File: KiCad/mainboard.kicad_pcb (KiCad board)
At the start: 2 copper layers, 139.7 x 83.8 mm, 60 parts, among them J1 Arduino_Nano_Header, P1 CONN_02X13, P2 CONN_02X13, P3 USB_B, P4 CONN_01X04, P5 CONN_01X02, P6 CONN_01X02, P7 CONN_01X02, U1 74LS165, U2 74LS165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

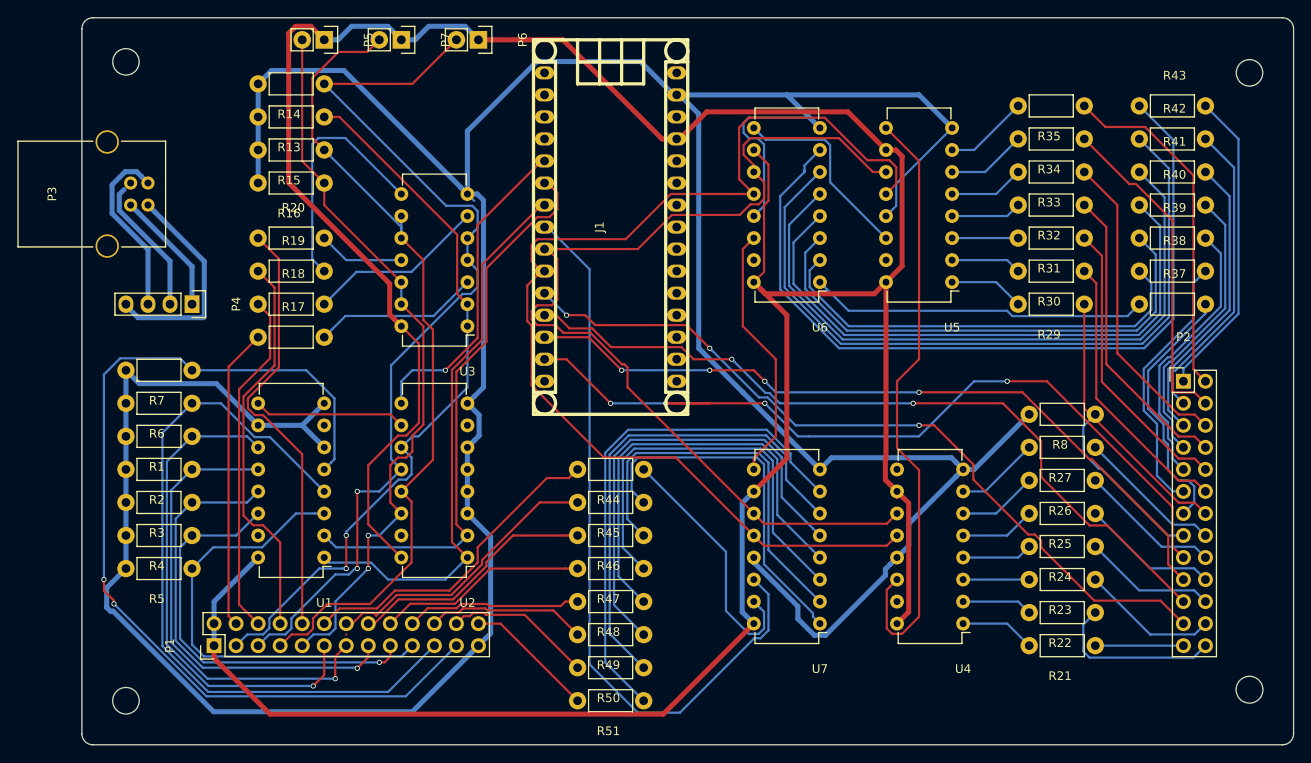
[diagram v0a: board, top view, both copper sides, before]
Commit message: turned Arduino around
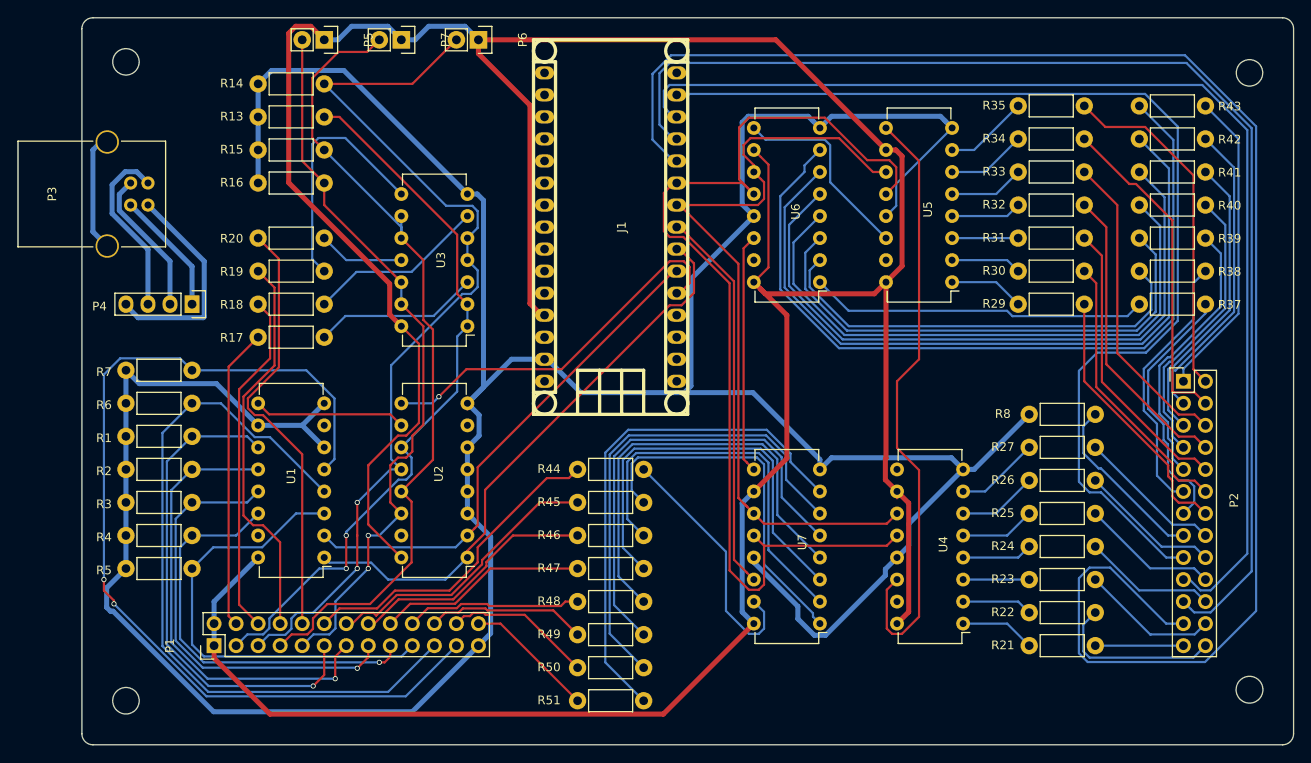
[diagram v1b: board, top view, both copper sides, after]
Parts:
- R8: value R -> 220R
- turned J1 to 90 degrees
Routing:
- net Net-(J1-Pad11): track 90.9 -> 188.3 mm, vias 3 -> 0
- net Net-(J1-Pad12): track 90.1 -> 142.6 mm, vias 2 -> 0
- net Net-(J1-Pad13): track 87.2 -> 132.0 mm, vias 4 -> 0
- net Net-(J1-Pad8): track 86.2 -> 44.5 mm
- net GND: track 438.8 -> 400.7 mm
- net VCC: track 369.6 -> 401.8 mm
- net Net-(J1-Pad14): track 96.3 -> 125.4 mm, vias 4 -> 0
- net Net-(J1-Pad9): track 118.1 -> 93.4 mm
- net Net-(P3-Pad5): track 0.00 -> 13.8 mm
- net Net-(J1-Pad10): track 129.1 -> 119.0 mm
- net Net-(J1-Pad6): track 65.2 -> 58.3 mm
- net Net-(J1-Pad5): track 37.2 -> 44.1 mm
- net Net-(U6-Pad14): track 29.8 -> 27.6 mm
- net Net-(J1-Pad7): track 64.6 -> 66.1 mm
- net Net-(P3-Pad3): track 15.9 -> 16.9 mm
